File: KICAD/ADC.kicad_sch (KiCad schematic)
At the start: 5 parts, among them IC3 PCM1808PW

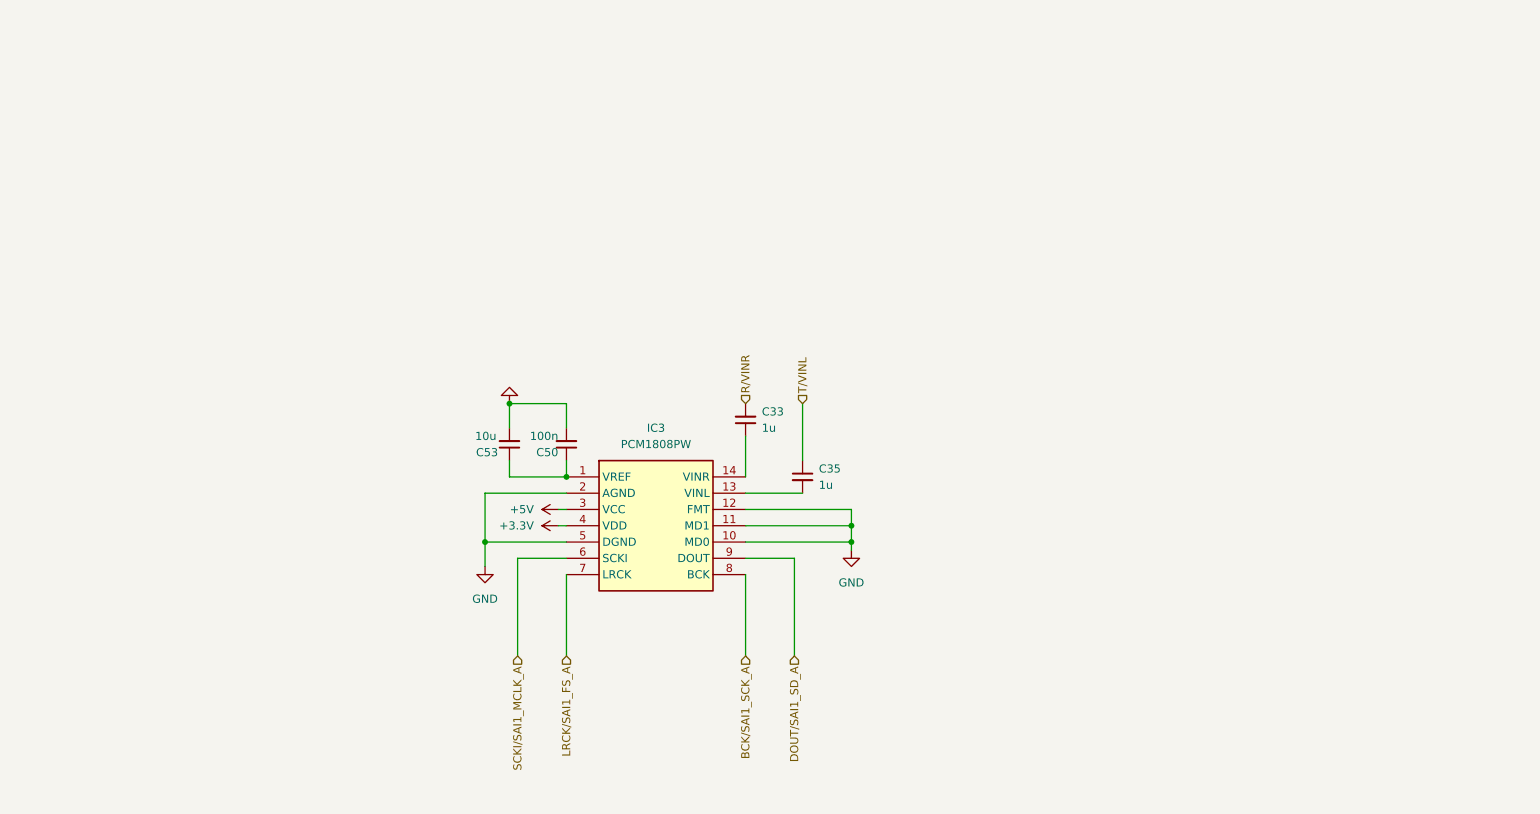
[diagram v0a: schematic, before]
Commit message: Proposition pour PCM1808
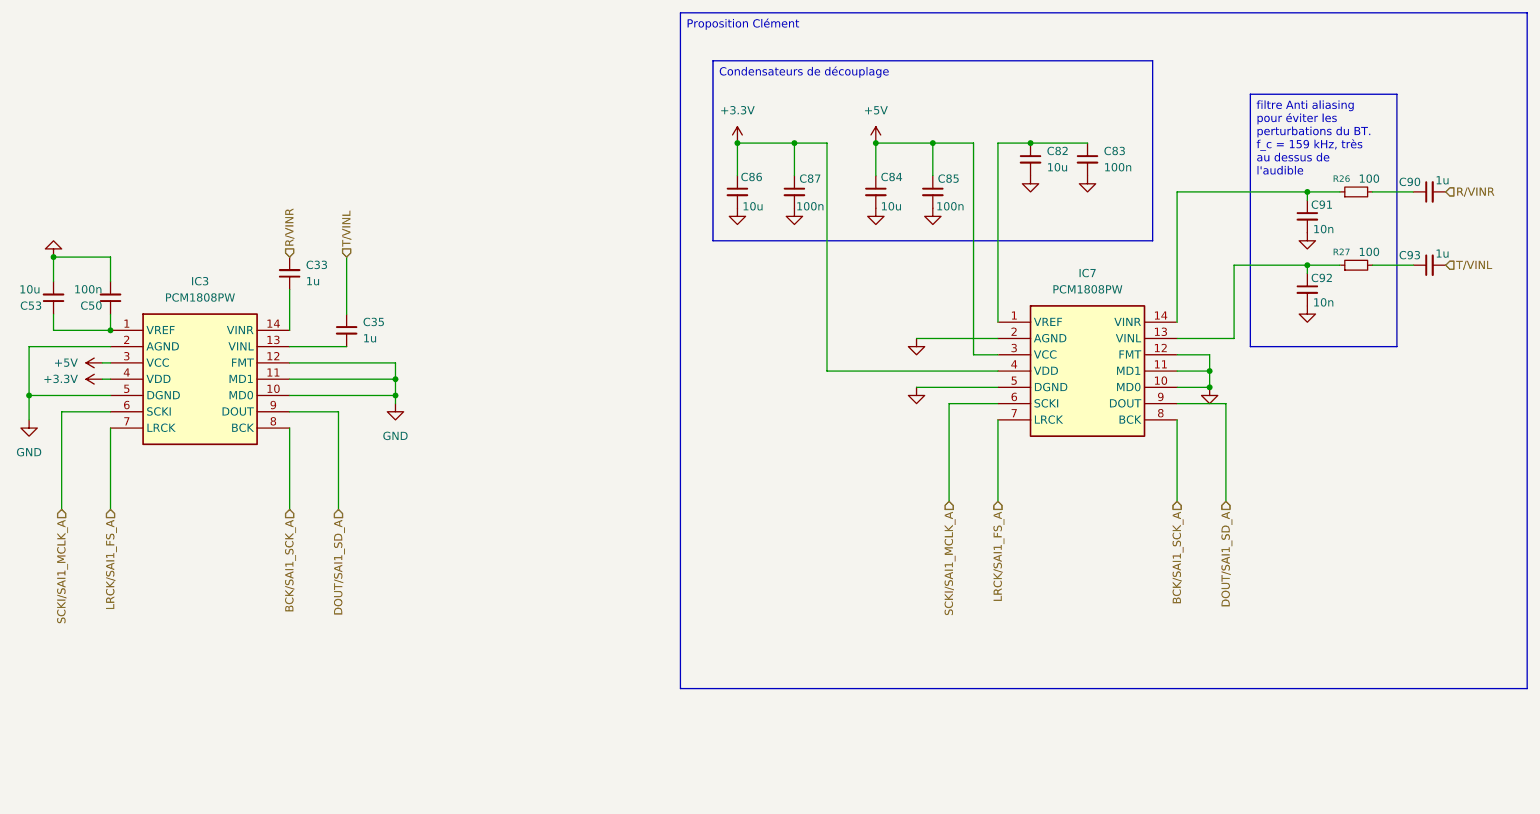
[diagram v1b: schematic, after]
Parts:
- added C82, C84, C86: 10u, symbol Device:C_Small
- added C83, C85, C87: 100n, symbol Device:C_Small
- added C90, C93: 1u, symbol Device:C_Small
- added C91, C92: 10n, symbol Device:C_Small
- added IC7: PCM1808PW, footprints:PCM1808PW, symbol PCM1808PW:PCM1808PW
- added R26, R27: 100, symbol Device:R_Small
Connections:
- net +3.3V: now also C86.1, C87.1, IC7.4 (VDD)
- net +5V: now also C84.1, C85.1, IC7.3 (VCC)
- net BCK/SAI1_SCK_A: now also IC7.8 (BCK)
- net DOUT/SAI1_SD_A: now also IC7.9 (DOUT)
- net GND: now also C82.2, C83.2, C84.2, C85.2, C86.2, C87.2, C91.2, C92.2, IC7.10 (MD0), IC7.11 (MD1), IC7.12 (FMT), IC7.2 (AGND), IC7.5 (DGND)
- net LRCK/SAI1_FS_A: now also IC7.7 (LRCK)
- net R/VINR: now also C90.2
- net SCKI/SAI1_MCLK_A: now also IC7.6 (SCKI)
- net T/VINL: now also C93.2
- new net: C82.1, C83.1, IC7.1 (VREF)
- new net: C92.1, IC7.13 (VINL), R27.1
- new net: C91.1, IC7.14 (VINR), R26.1
- new net: C93.1, R27.2
- new net: C90.1, R26.2
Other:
- moved on the sheet: C33, C35, C50, C53, IC3

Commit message: mise en forme globale
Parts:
- removed C33, C35: 1u, symbol Device:C_Small
- removed C50: 100n, symbol Device:C_Small
- removed C53: 10u, symbol Device:C_Small
- removed IC3: PCM1808PW, footprints:PCM1808PW, symbol PCM1808PW:PCM1808PW
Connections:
- net +3.3V renamed +3V3
- net BCK/SAI1_SCK_A renamed BCK
- net DOUT/SAI1_SD_A renamed DOUT
- net LRCK/SAI1_FS_A renamed LRCK
- net R/VINR renamed JACK_R
- net SCKI/SAI1_MCLK_A renamed SCKI
- net T/VINL renamed JACK_L
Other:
- moved on the sheet: C82, C83, C84, C85, C86, C87, C90, C91, C92, C93, IC7, R26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

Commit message: interface HM
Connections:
- net BCK renamed I2S_BCK
- net DOUT renamed I2S_DOUT
- net LRCK renamed I2S_LRCK
- net SCKI renamed I2S_SCKI
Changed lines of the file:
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@@
 		)
 	)
-	(hierarchical_label "DOUT"
+	(hierarchical_label "I2S_DOUT"
 		(shape input)
 		(at 161.29 100.33 270)
@@
 		)
 	)
-	(hierarchical_label "LRCK"
+	(hierarchical_label "I2S_LRCK"
 		(shape input)
 		(at 125.73 100.33 270)
@@
 		)
 	)
-	(hierarchical_label "BCK"
+	(hierarchical_label "I2S_BCK"
 		(shape input)
 		(at 153.67 100.33 270)
@@
 		)
 	)
-	(hierarchical_label "SCKI"
+	(hierarchical_label "I2S_SCKI"
 		(shape input)
 		(at 118.11 100.33 270)
